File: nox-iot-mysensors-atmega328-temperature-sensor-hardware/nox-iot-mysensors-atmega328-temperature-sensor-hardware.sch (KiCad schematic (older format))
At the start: 12 parts, among them J1 Conn_01x03, J2 FTDI232, J3 AHT10, U1 ATmega328P-PU, U2 WAVGAT 3.3V, U3 NRF24L01+, Y1 16 MHZ

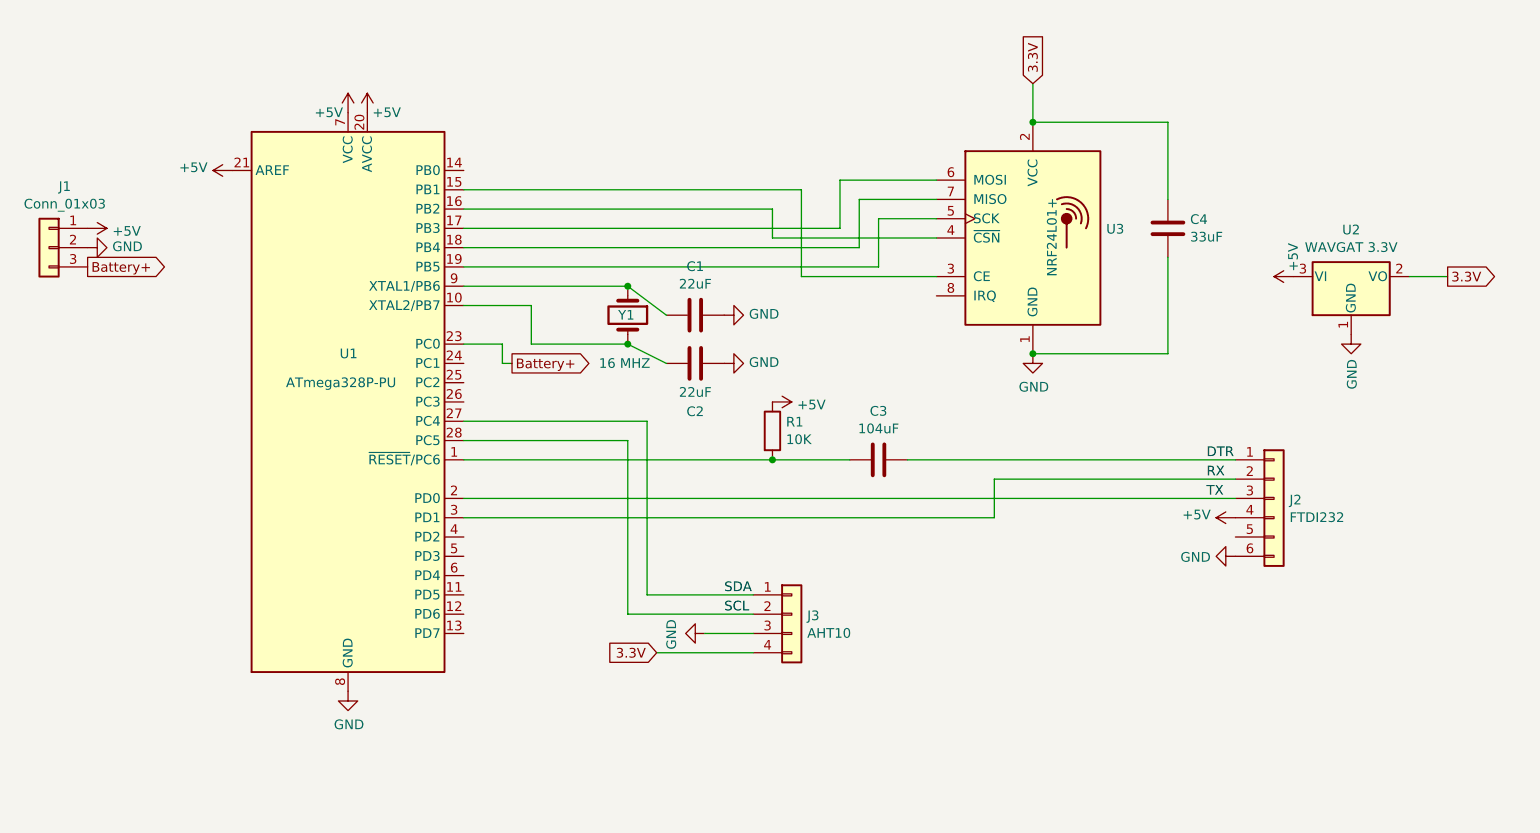
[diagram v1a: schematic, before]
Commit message: components in place
before wiring components por perfboard
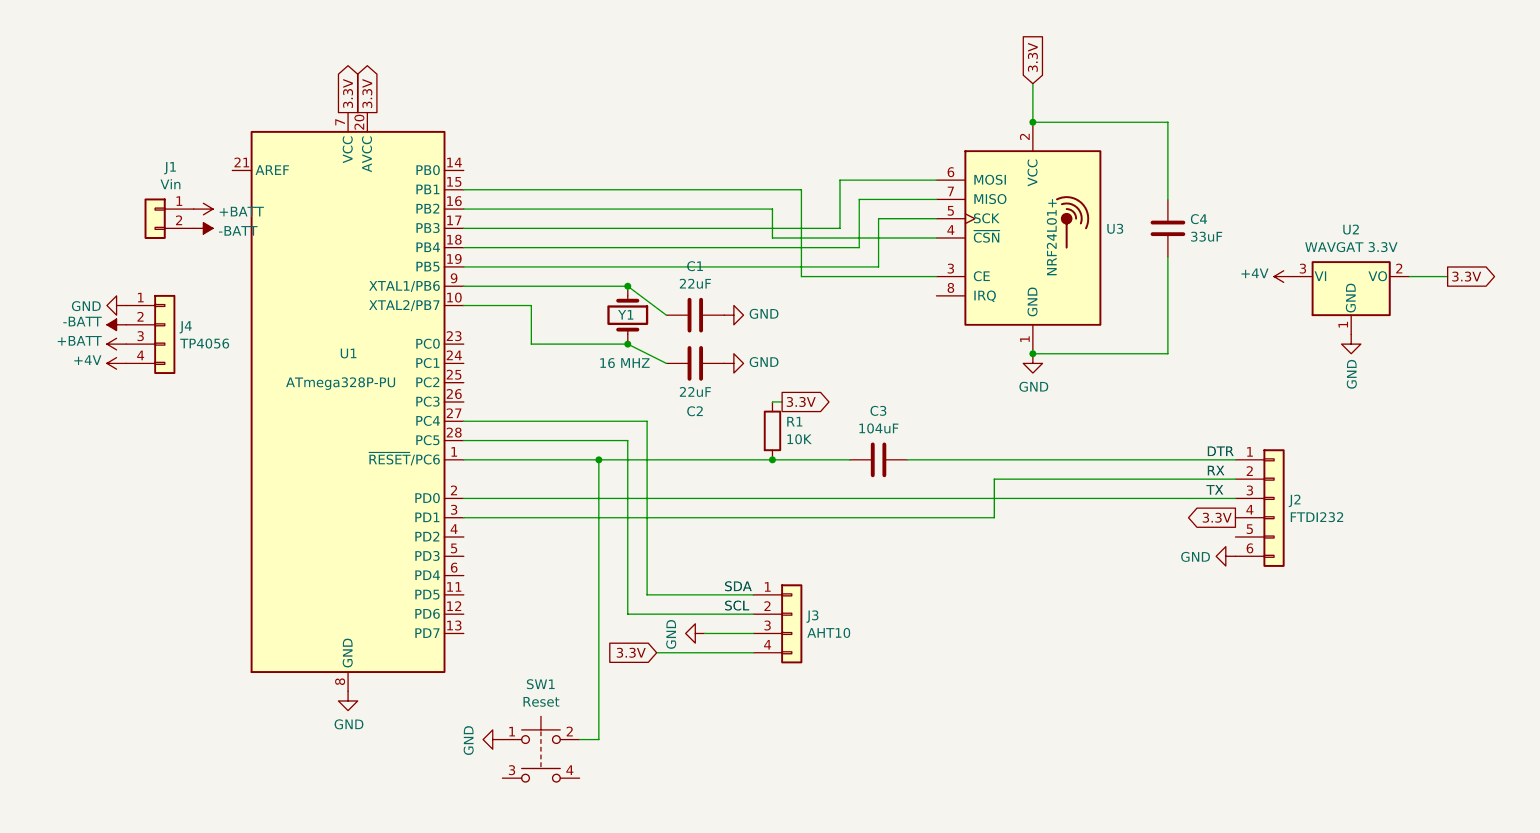
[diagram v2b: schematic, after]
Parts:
- removed J1: Conn_01x03, Connector_JST:JST_EH_B3B-EH-A_1x03_P2.50mm_Vertical, symbol Connector_Generic:Conn_01x03
- added J1: Vin, Connector_JST:JST_EH_B2B-EH-A_1x02_P2.50mm_Vertical, symbol Connector_Generic:Conn_01x02
- added J4: TP4056, Connector_PinSocket_2.54mm:PinSocket_1x04_P2.54mm_Vertical, symbol Connector_Generic:Conn_01x04
- added SW1: Reset, Button_Switch_THT:SW_TH_Tactile_Omron_B3F-10xx, symbol Switch:SW_Push_Dual
- U1: footprint Package_DIP:DIP-28_W7.62mm -> Package_DIP:DIP-28_W7.62mm_Socket
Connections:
- net 3.3V: now also J2.4 (Pin_4), R1.1, U1.20 (AVCC), U1.7 (VCC)
- net GND: now also J4.1 (Pin_1), SW1.1
- net at C3.2, R1.2, U1.1 (~RESET~/PC6): now also SW1.2
- removed net +5V: J2.4 (Pin_4), R1.1, U1.20 (AVCC), U1.21 (AREF), U1.7 (VCC), U2.3 (VI)
- net Battery+: no longer names the net of U1.23 (PC0)
- new net +4V: J4.4 (Pin_4), U2.3 (VI)
- new net +BATT: J1.1 (Pin_1), J4.3 (Pin_3)
- new net -BATT: J1.2 (Pin_2), J4.2 (Pin_2)
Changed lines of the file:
@@
 F 0 "U1" H 3450 2800 50  0000 R CNN
 F 1 "ATmega328P-PU" H 3650 2650 50  0000 R CNN
-F 2 "Package_DIP:DIP-28_W7.62mm" H 3400 2550 50  0001 C CIN
+F 2 "Package_DIP:DIP-28_W7.62mm_Socket" H 3400 2550 50  0001 C CIN
 F 3 "http://ww1.microchip.com/downloads/en/DeviceDoc/ATmega328_P%20AVR%20MCU%20with%20picoPower%20Technology%20Data%20Sheet%2040001984A.pdf" H 3400 2550 50  0001 C CNN
 	1    3400 2550
@@
 $EndComp
 $Comp
-L power:+5V #PWR0108
-U 1 1 5E1F682D
-P 3400 1050
-F 0 "#PWR0108" H 3400 900 50  0001 C CNN
-F 1 "+5V" H 3300 1050 50  0000 C CNN
-F 2 "" H 3400 1050 50  0001 C CNN
-F 3 "" H 3400 1050 50  0001 C CNN
-	1    3400 1050
-	1    0    0    -1
-$EndComp
-$Comp
-L power:+5V #PWR0109
-U 1 1 5E1FA370
-P 2800 1350
-F 0 "#PWR0109" H 2800 1200 50  0001 C CNN
-F 1 "+5V" V 2815 1478 50  0000 L CNN
-F 2 "" H 2800 1350 50  0001 C CNN
-F 3 "" H 2800 1350 50  0001 C CNN
-	1    2800 1350
-	0    -1   -1   0
-$EndComp
-$Comp
-L power:+5V #PWR0111
-U 1 1 5E1FCC86
-P 3500 1050
-F 0 "#PWR0111" H 3500 900 50  0001 C CNN
-F 1 "+5V" H 3600 1050 50  0000 C CNN
-F 2 "" H 3500 1050 50  0001 C CNN
-F 3 "" H 3500 1050 50  0001 C CNN
-	1    3500 1050
-	1    0    0    -1
-$EndComp
-$Comp
 L Connector_Generic:Conn_01x06 J2
 U 1 1 5E1FE269
@@
 $EndComp
 $Comp
-L power:+5V #PWR0112
-U 1 1 5E2033C2
-P 8000 3150
-F 0 "#PWR0112" H 8000 3000 50  0001 C CNN
-F 1 "+5V" V 8015 3278 50  0000 L CNN
-F 2 "" H 8000 3150 50  0001 C CNN
-F 3 "" H 8000 3150 50  0001 C CNN
-	1    8000 3150
-	0    -1   -1   0
-$EndComp
-$Comp
 L power:GND #PWR0113
 U 1 1 5E2039CD
@@
 $EndComp
 $Comp
-L power:+5V #PWR0114
-U 1 1 5E22D728
-P 5600 2550
-F 0 "#PWR0114" H 5600 2400 50  0001 C CNN
-F 1 "+5V" V 5615 2678 50  0000 L CNN
-F 2 "" H 5600 2550 50  0001 C CNN
-F 3 "" H 5600 2550 50  0001 C CNN
-	1    5600 2550
-	0    1    1    0
-$EndComp
-$Comp
 L Device:C C3
 U 1 1 5E1B5344
@@
 Connection ~ 5600 2850
 Wire Wire Line
-	4000 2850 5600 2850
+	4000 2850 4700 2850
 Wire Wire Line
 	4000 3150 6750 3150
@@
 Text Label 7850 3050 0    50   ~ 0
 TX
+Connection ~ 6950 1100
+Wire Wire Line
+	6950 900  6950 1100
+$Comp
+L power:GND #PWR01
+U 1 1 5E2F2798
+P 5250 3750
+F 0 "#PWR01" H 5250 3500 50  0001 C CNN
+F 1 "GND" H 5255 3577 50  0000 C CNN
+F 2 "" H 5250 3750 50  0001 C CNN
+F 3 "" H 5250 3750 50  0001 C CNN
+	1    5250 3750
+	0    1    1    0
+$EndComp
+Wire Wire Line
+	5250 3750 5500 3750
+Wire Wire Line
+	4000 2750 4850 2750
+Wire Wire Line
+	4850 2750 4850 3650
+Wire Wire Line
+	4850 3650 5500 3650
+Wire Wire Line
+	4000 2650 4950 2650
+Wire Wire Line
+	4950 2650 4950 3550
+Wire Wire Line
+	4950 3550 5500 3550
+Text Label 5350 3550 0    50   ~ 0
+SDA
+Text Label 5350 3650 0    50   ~ 0
+SCL
+$Comp
+L Connector_Generic:Conn_01x04 J3
+U 1 1 5E2EC327
+P 5700 3650
+F 0 "J3" H 5780 3642 50  0000 L CNN
+F 1 "AHT10" H 5780 3551 50  0000 L CNN
+F 2 "Connector_PinSocket_2.54mm:PinSocket_1x04_P2.54mm_Vertical" H 5700 3650 50  0001 C CNN
+F 3 "~" H 5700 3650 50  0001 C CNN
+	1    5700 3650
+	1    0    0    -1
+$EndComp
+$Comp
+L Connector_Generic:Conn_01x02 J1
+U 1 1 5E3624A5
+P 2400 1550
+F 0 "J1" H 2318 1767 50  0000 C CNN
+F 1 "Vin" H 2318 1676 50  0000 C CNN
+F 2 "Connector_JST:JST_EH_B2B-EH-A_1x02_P2.50mm_Vertical" H 2400 1550 50  0001 C CNN
+F 3 "~" H 2400 1550 50  0001 C CNN
+	1    2400 1550
+	-1   0    0    -1
+$EndComp
+$Comp
+L Switch:SW_Push_Dual SW1
+U 1 1 5E36B497
+P 4400 4300
+F 0 "SW1" H 4400 4585 50  0000 C CNN
+F 1 "Reset" H 4400 4494 50  0000 C CNN
+F 2 "Button_Switch_THT:SW_TH_Tactile_Omron_B3F-10xx" H 4400 4500 50  0001 C CNN
+F 3 "~" H 4400 4500 50  0001 C CNN
+	1    4400 4300
+	1    0    0    -1
+$EndComp
+$Comp
+L power:GND #PWR06
+U 1 1 5E36ED7A
+P 4200 4300
+F 0 "#PWR06" H 4200 4050 50  0001 C CNN
+F 1 "GND" H 4205 4127 50  0000 C CNN
+F 2 "" H 4200 4300 50  0001 C CNN
+F 3 "" H 4200 4300 50  0001 C CNN
+	1    4200 4300
+	0    1    1    0
+$EndComp
+Wire Wire Line
+	4700 2850 4700 4300
+Wire Wire Line
+	4700 4300 4600 4300
+Connection ~ 4700 2850
+Wire Wire Line
+	4700 2850 5600 2850
+Wire Wire Line
+	5500 3850 5000 3850
+Text GLabel 5000 3850 0    50   Input ~ 0
+3.3V
 Text GLabel 6950 900  1    50   Input ~ 0
 3.3V
-Connection ~ 6950 1100
-Wire Wire Line
-	6950 900  6950 1100
+Wire Wire Line
+	8900 1900 9100 1900
+Text GLabel 9100 1900 2    50   Output ~ 0
+3.3V
+$Comp
+L power:GND #PWR03
+U 1 1 5E2E0195
+P 8600 2200
+F 0 "#PWR03" H 8600 1950 50  0001 C CNN
+F 1 "GND" V 8605 2072 50  0000 R CNN
+F 2 "" H 8600 2200 50  0001 C CNN
+F 3 "" H 8600 2200 50  0001 C CNN
+	1    8600 2200
+	1    0    0    -1
+$EndComp
 $Comp
 L Regulator_Linear:LM1117-3.3 U2
@@
 	1    0    0    -1
 $EndComp
-$Comp
-L power:+5V #PWR02
-U 1 1 5E2DFBC7
+Text GLabel 3500 1050 1    50   Output ~ 0
+3.3V
+Text GLabel 3400 1050 1    50   Output ~ 0
+3.3V
+Text GLabel 8000 3150 0    50   Output ~ 0
+3.3V
+Text GLabel 5650 2550 2    50   Output ~ 0
+3.3V
+Wire Wire Line
+	5600 2550 5650 2550
+$Comp
+L Connector_Generic:Conn_01x04 J4
+U 1 1 5E764A8C
+P 2450 2150
+F 0 "J4" H 2530 2142 50  0000 L CNN
+F 1 "TP4056" H 2530 2051 50  0000 L CNN
+F 2 "Connector_PinSocket_2.54mm:PinSocket_1x04_P2.54mm_Vertical" H 2450 2150 50  0001 C CNN
+F 3 "~" H 2450 2150 50  0001 C CNN
+	1    2450 2150
+	1    0    0    -1
+$EndComp
+$Comp
+L power:GND #PWR09
+U 1 1 5E768EE0
+P 2250 2050
+F 0 "#PWR09" H 2250 1800 50  0001 C CNN
+F 1 "GND" V 2255 1922 50  0000 R CNN
+F 2 "" H 2250 2050 50  0001 C CNN
+F 3 "" H 2250 2050 50  0001 C CNN
+	1    2250 2050
+	0    1    1    0
+$EndComp
+$Comp
+L power:+4V #PWR0107
+U 1 1 5E77A1CA
 P 8300 1900
-F 0 "#PWR02" H 8300 1750 50  0001 C CNN
-F 1 "+5V" H 8400 1900 50  0000 C CNN
+F 0 "#PWR0107" H 8300 1750 50  0001 C CNN
+F 1 "+4V" V 8315 2028 50  0000 L CNN
 F 2 "" H 8300 1900 50  0001 C CNN
 F 3 "" H 8300 1900 50  0001 C CNN
@@
 $EndComp
 $Comp
-L power:GND #PWR03
-U 1 1 5E2E0195
-P 8600 2200
-F 0 "#PWR03" H 8600 1950 50  0001 C CNN
-F 1 "GND" V 8605 2072 50  0000 R CNN
-F 2 "" H 8600 2200 50  0001 C CNN
-F 3 "" H 8600 2200 50  0001 C CNN
-	1    8600 2200
-	1    0    0    -1
-$EndComp
-Text GLabel 9100 1900 2    50   Output ~ 0
-3.3V
-Wire Wire Line
-	8900 1900 9100 1900
-Text GLabel 5000 3850 0    50   Input ~ 0
-3.3V
-Wire Wire Line
-	5500 3850 5000 3850
-$Comp
-L power:GND #PWR01
-U 1 1 5E2F2798
-P 5250 3750
-F 0 "#PWR01" H 5250 3500 50  0001 C CNN
-F 1 "GND" H 5255 3577 50  0000 C CNN
-F 2 "" H 5250 3750 50  0001 C CNN
-F 3 "" H 5250 3750 50  0001 C CNN
-	1    5250 3750
-	0    1    1    0
-$EndComp
-Wire Wire Line
-	5250 3750 5500 3750
-Wire Wire Line
-	4000 2750 4850 2750
-Wire Wire Line
-	4850 2750 4850 3650
-Wire Wire Line
-	4850 3650 5500 3650
-Wire Wire Line
-	4000 2650 4950 2650
-Wire Wire Line
-	4950 2650 4950 3550
-Wire Wire Line
-	4950 3550 5500 3550
-Text Label 5350 3550 0    50   ~ 0
-SDA
-Text Label 5350 3650 0    50   ~ 0
-SCL
-$Comp
-L Connector_Generic:Conn_01x03 J1
-U 1 1 5E2E1CFC
-P 1850 1750
-F 0 "J1" H 1768 2067 50  0000 C CNN
-F 1 "Conn_01x03" H 1768 1976 50  0000 C CNN
-F 2 "Connector_JST:JST_EH_B3B-EH-A_1x03_P2.50mm_Vertical" H 1850 1750 50  0001 C CNN
-F 3 "~" H 1850 1750 50  0001 C CNN
-	1    1850 1750
-	-1   0    0    -1
-$EndComp
-$Comp
-L power:+5V #PWR04
-U 1 1 5E2E3230
-P 2050 1650
-F 0 "#PWR04" H 2050 1500 50  0001 C CNN
-F 1 "+5V" V 2065 1778 50  0000 L CNN
-F 2 "" H 2050 1650 50  0001 C CNN
-F 3 "" H 2050 1650 50  0001 C CNN
-	1    2050 1650
-	0    1    1    0
-$EndComp
-$Comp
-L power:GND #PWR05
-U 1 1 5E2E3606
-P 2050 1750
-F 0 "#PWR05" H 2050 1500 50  0001 C CNN
-F 1 "GND" V 2055 1622 50  0000 R CNN
-F 2 "" H 2050 1750 50  0001 C CNN
-F 3 "" H 2050 1750 50  0001 C CNN
-	1    2050 1750
-	0    -1   -1   0
-$EndComp
-Text GLabel 2050 1850 2    50   Output ~ 0
-Battery+
-Text GLabel 4250 2350 2    50   Output ~ 0
-Battery+
-Wire Wire Line
-	4250 2350 4200 2350
-Wire Wire Line
-	4200 2350 4200 2250
-Wire Wire Line
-	4200 2250 4000 2250
-$Comp
-L Connector_Generic:Conn_01x04 J3
-U 1 1 5E2EC327
-P 5700 3650
-F 0 "J3" H 5780 3642 50  0000 L CNN
-F 1 "AHT10" H 5780 3551 50  0000 L CNN
-F 2 "Connector_PinSocket_2.54mm:PinSocket_1x04_P2.54mm_Vertical" H 5700 3650 50  0001 C CNN
-F 3 "~" H 5700 3650 50  0001 C CNN
-	1    5700 3650
-	1    0    0    -1
+L power:+4V #PWR0108
+U 1 1 5E77B602
+P 2250 2350
+F 0 "#PWR0108" H 2250 2200 50  0001 C CNN
+F 1 "+4V" V 2265 2478 50  0000 L CNN
+F 2 "" H 2250 2350 50  0001 C CNN
+F 3 "" H 2250 2350 50  0001 C CNN
+	1    2250 2350
+	0    -1   -1   0
+$EndComp
+$Comp
+L power:+BATT #PWR?
+U 1 1 5E783316
+P 2600 1550
+F 0 "#PWR?" H 2600 1400 50  0001 C CNN
+F 1 "+BATT" V 2615 1678 50  0000 L CNN
+F 2 "" H 2600 1550 50  0001 C CNN
+F 3 "" H 2600 1550 50  0001 C CNN
+	1    2600 1550
+	0    1    1    0
+$EndComp
+$Comp
+L power:+BATT #PWR?
+U 1 1 5E78700E
+P 2250 2250
+F 0 "#PWR?" H 2250 2100 50  0001 C CNN
+F 1 "+BATT" V 2265 2377 50  0000 L CNN
+F 2 "" H 2250 2250 50  0001 C CNN
+F 3 "" H 2250 2250 50  0001 C CNN
+	1    2250 2250
+	0    -1   -1   0
+$EndComp
+$Comp
+L power:-BATT #PWR?
+U 1 1 5E787B63
+P 2600 1650
+F 0 "#PWR?" H 2600 1500 50  0001 C CNN
+F 1 "-BATT" V 2615 1778 50  0000 L CNN
+F 2 "" H 2600 1650 50  0001 C CNN
+F 3 "" H 2600 1650 50  0001 C CNN
+	1    2600 1650
+	0    1    1    0
+$EndComp
+$Comp
+L power:-BATT #PWR?
+U 1 1 5E788B81
+P 2250 2150
+F 0 "#PWR?" H 2250 2000 50  0001 C CNN
+F 1 "-BATT" V 2265 2277 50  0000 L CNN
+F 2 "" H 2250 2150 50  0001 C CNN
+F 3 "" H 2250 2150 50  0001 C CNN
+	1    2250 2150
+	0    -1   -1   0
 $EndComp
 $EndSCHEMATC

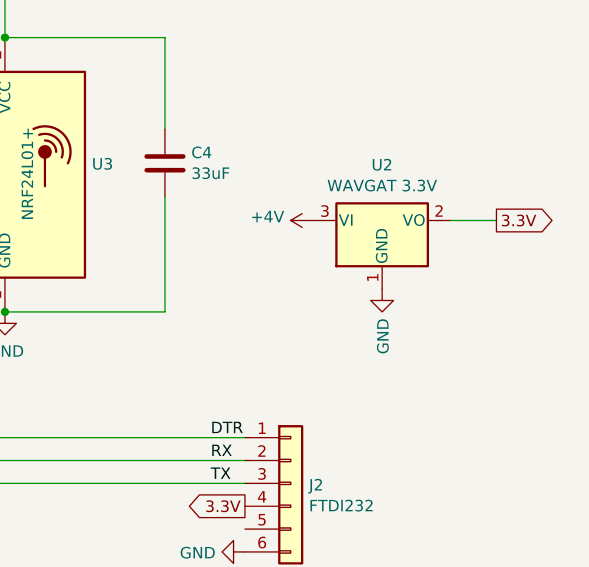
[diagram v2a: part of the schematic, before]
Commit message: wires complete for perfboard
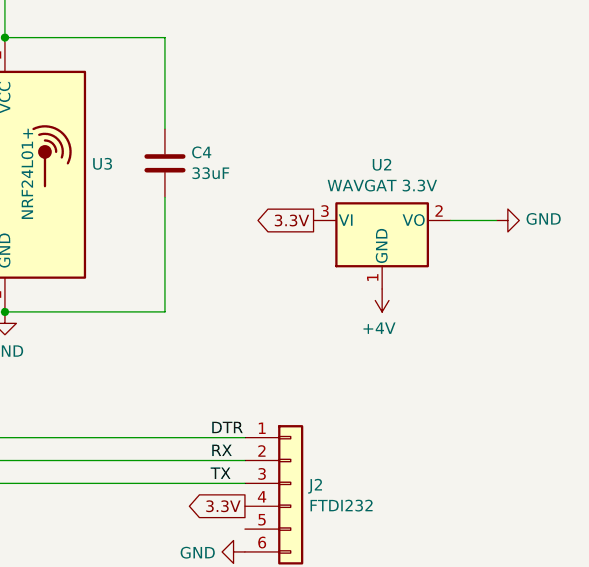
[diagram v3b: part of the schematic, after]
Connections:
- net +4V: now also U2.1 (GND); no longer U2.3 (VI)
- net 3.3V: now also U2.3 (VI); no longer U2.2 (VO)
- net GND: now also U2.2 (VO); no longer U2.1 (GND)
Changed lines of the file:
@@
 Wire Wire Line
 	8900 1900 9100 1900
-Text GLabel 9100 1900 2    50   Output ~ 0
+Text GLabel 8300 1900 0    50   Output ~ 0
 3.3V
 $Comp
 L power:GND #PWR03
 U 1 1 5E2E0195
-P 8600 2200
-F 0 "#PWR03" H 8600 1950 50  0001 C CNN
-F 1 "GND" V 8605 2072 50  0000 R CNN
-F 2 "" H 8600 2200 50  0001 C CNN
-F 3 "" H 8600 2200 50  0001 C CNN
-	1    8600 2200
-	1    0    0    -1
+P 9100 1900
+F 0 "#PWR03" H 9100 1650 50  0001 C CNN
+F 1 "GND" V 9105 1772 50  0000 R CNN
+F 2 "" H 9100 1900 50  0001 C CNN
+F 3 "" H 9100 1900 50  0001 C CNN
+	1    9100 1900
+	0    -1   -1   0
 $EndComp
 $Comp
@@
 L power:+4V #PWR0107
 U 1 1 5E77A1CA
-P 8300 1900
-F 0 "#PWR0107" H 8300 1750 50  0001 C CNN
-F 1 "+4V" V 8315 2028 50  0000 L CNN
-F 2 "" H 8300 1900 50  0001 C CNN
-F 3 "" H 8300 1900 50  0001 C CNN
-	1    8300 1900
-	0    -1   -1   0
+P 8600 2200
+F 0 "#PWR0107" H 8600 2050 50  0001 C CNN
+F 1 "+4V" H 8615 2373 50  0000 C CNN
+F 2 "" H 8600 2200 50  0001 C CNN
+F 3 "" H 8600 2200 50  0001 C CNN
+	1    8600 2200
+	-1   0    0    1
 $EndComp
 $Comp
@@
 $EndComp
 $Comp
-L power:+BATT #PWR?
+L power:+BATT #PWR0104
 U 1 1 5E783316
 P 2600 1550
-F 0 "#PWR?" H 2600 1400 50  0001 C CNN
+F 0 "#PWR0104" H 2600 1400 50  0001 C CNN
 F 1 "+BATT" V 2615 1678 50  0000 L CNN
 F 2 "" H 2600 1550 50  0001 C CNN
@@
 $EndComp
 $Comp
-L power:+BATT #PWR?
+L power:+BATT #PWR0106
 U 1 1 5E78700E
 P 2250 2250
-F 0 "#PWR?" H 2250 2100 50  0001 C CNN
+F 0 "#PWR0106" H 2250 2100 50  0001 C CNN
 F 1 "+BATT" V 2265 2377 50  0000 L CNN
 F 2 "" H 2250 2250 50  0001 C CNN
@@
 $EndComp
 $Comp
-L power:-BATT #PWR?
+L power:-BATT #PWR0109
 U 1 1 5E787B63
 P 2600 1650
-F 0 "#PWR?" H 2600 1500 50  0001 C CNN
+F 0 "#PWR0109" H 2600 1500 50  0001 C CNN
 F 1 "-BATT" V 2615 1778 50  0000 L CNN
 F 2 "" H 2600 1650 50  0001 C CNN
@@
 $EndComp
 $Comp
-L power:-BATT #PWR?
+L power:-BATT #PWR0110
 U 1 1 5E788B81
 P 2250 2150
-F 0 "#PWR?" H 2250 2000 50  0001 C CNN
+F 0 "#PWR0110" H 2250 2000 50  0001 C CNN
 F 1 "-BATT" V 2265 2277 50  0000 L CNN
 F 2 "" H 2250 2150 50  0001 C CNN
